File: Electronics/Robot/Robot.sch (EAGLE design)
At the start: 23 parts, among them Q1 2N7000, Q2 2N7000, U1 GY-521MPU6050, U2 SN74LS241N

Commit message: Fixed Gears and made PCB
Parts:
- removed JP1: B3B-PH-K-S, con-JST PH:B3B-PH-K-S
- added X2: JST-XH-03-PIN-ROUND-PAD, JST XH Connectors v1-0:JST-XH-03-PIN-ROUND-PAD
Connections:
- net ENABLE_AX12: now also U$1.20/A6/TX5
- net GND: now also X2-3.S; no longer JP1.3
- net RX_AX12: now also U$1.17/A3/TX4/SDA1
- net SSC-32-RX: now also X2-2.S; no longer JP1.2
- net SSC-32-TX: now also X2-1.S; no longer JP1.1
- net TX_AX12: now also U$1.16/A2/RX4/SCL1
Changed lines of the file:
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@@
 <?xml version="1.0" encoding="utf-8"?>
 <!DOCTYPE eagle SYSTEM "eagle.dtd">
-<eagle version="9.6.1">
+<eagle version="9.6.2">
 <drawing>
 <settings>
@@
 <part name="+3V4" library="supply1" library_urn="urn:adsk.eagle:library:371" deviceset="+3V3" device=""/>
 <part name="P+4" library="supply1" library_urn="urn:adsk.eagle:library:371" deviceset="+5V" device=""/>
-<part name="JP1" library="con-JST PH" deviceset="B3B-PH" device="-K-S"/>
 <part name="GND1" library="supply1" library_urn="urn:adsk.eagle:library:371" deviceset="GND" device=""/>
 <part name="H1" library="holes" library_urn="urn:adsk.eagle:library:237" deviceset="MOUNT-HOLE" device="3.0" package3d_urn="urn:adsk.eagle:package:14277/1"/>
@@
 <part name="GND4" library="supply1" library_urn="urn:adsk.eagle:library:371" deviceset="GND" device=""/>
 <part name="U$1" library="Teensy_3_and_LC_Series_Boards_v1.4" deviceset="TEENSY_4.0" device=""/>
+<part name="X2" library="JST XH Connectors v1-0" deviceset="JST-XH-03-PIN" device="-ROUND-PAD"/>
 </parts>
 <sheets>
@@
 <attribute name="VALUE" x="299.72" y="238.76" size="1.778" layer="96" rot="R90"/>
 </instance>
-<instance part="JP1" gate="G$1" x="358.14" y="149.86" smashed="yes" rot="R180">
-<attribute name="NAME" x="364.49" y="144.145" size="1.778" layer="95" rot="R180"/>
-<attribute name="VALUE" x="364.49" y="157.48" size="1.778" layer="96" rot="R180"/>
-</instance>
 <instance part="GND1" gate="1" x="345.44" y="137.16" smashed="yes" rot="MR0">
 <attribute name="VALUE" x="347.98" y="134.62" size="1.778" layer="96" rot="MR0"/>
@@
 <attribute name="NAME" x="52.832" y="229.87" size="1.27" layer="95" font="vector" ratio="15"/>
 <attribute name="VALUE" x="55.626" y="157.48" size="1.27" layer="96" font="vector" ratio="15"/>
+</instance>
+<instance part="X2" gate="-1" x="353.06" y="152.4" smashed="yes">
+<attribute name="NAME" x="355.6" y="151.638" size="1.524" layer="95"/>
+<attribute name="VALUE" x="352.298" y="153.797" size="1.778" layer="96"/>
+</instance>
+<instance part="X2" gate="-2" x="353.06" y="149.86" smashed="yes">
+<attribute name="NAME" x="355.6" y="149.098" size="1.524" layer="95"/>
+</instance>
+<instance part="X2" gate="-3" x="353.06" y="147.32" smashed="yes">
+<attribute name="NAME" x="355.6" y="146.558" size="1.524" layer="95"/>
 </instance>
 </instances>
@@
 <pinref part="GND1" gate="1" pin="GND"/>
 <wire x1="345.44" y1="139.7" x2="345.44" y2="147.32" width="0.1524" layer="91"/>
-<pinref part="JP1" gate="G$1" pin="3"/>
 <wire x1="345.44" y1="147.32" x2="350.52" y2="147.32" width="0.1524" layer="91"/>
+<pinref part="X2" gate="-3" pin="S"/>
 </segment>
 <segment>
@@
 <net name="SSC-32-RX" class="0">
 <segment>
-<pinref part="JP1" gate="G$1" pin="2"/>
 <wire x1="350.52" y1="149.86" x2="345.44" y2="149.86" width="0.1524" layer="91"/>
 <label x="345.44" y="149.86" size="1.016" layer="95" rot="R180" xref="yes"/>
+<pinref part="X2" gate="-2" pin="S"/>
 </segment>
 <segment>
@@
 <net name="SSC-32-TX" class="0">
 <segment>
-<pinref part="JP1" gate="G$1" pin="1"/>
 <wire x1="350.52" y1="152.4" x2="345.44" y2="152.4" width="0.1524" layer="91"/>
 <label x="345.44" y="152.4" size="1.016" layer="95" rot="R180" xref="yes"/>
+<pinref part="X2" gate="-1" pin="S"/>
 </segment>
 <segment>
@@
 <label x="27.94" y="165.1" size="1.016" layer="95" rot="R180" xref="yes"/>
 <pinref part="U$1" gate="G$1" pin="23/A9/PWM"/>
+</segment>
+</net>
+<net name="TX_AX12" class="0">
+<segment>
+<pinref part="U$1" gate="G$1" pin="16/A2/RX4/SCL1"/>
+<wire x1="35.56" y1="182.88" x2="27.94" y2="182.88" width="0.1524" layer="91"/>
+<label x="27.94" y="182.88" size="1.016" layer="95" rot="R180" xref="yes"/>
+</segment>
+</net>
+<net name="RX_AX12" class="0">
+<segment>
+<pinref part="U$1" gate="G$1" pin="17/A3/TX4/SDA1"/>
+<wire x1="35.56" y1="180.34" x2="27.94" y2="180.34" width="0.1524" layer="91"/>
+<label x="27.94" y="180.34" size="1.016" layer="95" rot="R180" xref="yes"/>
+</segment>
+</net>
+<net name="ENABLE_AX12" class="0">
+<segment>
+<pinref part="U$1" gate="G$1" pin="20/A6/TX5"/>
+<wire x1="35.56" y1="172.72" x2="27.94" y2="172.72" width="0.1524" layer="91"/>
+<label x="27.94" y="172.72" size="1.016" layer="95" rot="R180" xref="yes"/>
 </segment>
 </net>
@@
 <wire x1="127" y1="175.26" x2="127" y2="132.08" width="0.1524" layer="91"/>
 <wire x1="127" y1="132.08" x2="165.1" y2="132.08" width="0.1524" layer="91"/>
-<label x="101.6" y="175.26" size="1.778" layer="95"/>
+<label x="96.52" y="175.26" size="1.778" layer="95" rot="R180" xref="yes"/>
 </segment>
 </net>
@@
 <wire x1="121.92" y1="170.18" x2="121.92" y2="114.3" width="0.1524" layer="91"/>
 <wire x1="96.52" y1="170.18" x2="121.92" y2="170.18" width="0.1524" layer="91"/>
-<label x="101.6" y="170.18" size="1.778" layer="95"/>
 <wire x1="203.2" y1="114.3" x2="203.2" y2="165.1" width="0.1524" layer="91"/>
 <pinref part="U2" gate="A" pin="1Y1"/>
 <wire x1="203.2" y1="165.1" x2="200.66" y2="165.1" width="0.1524" layer="91"/>
 <wire x1="121.92" y1="114.3" x2="203.2" y2="114.3" width="0.1524" layer="91"/>
+<label x="96.52" y="170.18" size="1.778" layer="95" rot="R180" xref="yes"/>
 </segment>
 </net>
@@
 <wire x1="162.56" y1="157.48" x2="165.1" y2="157.48" width="0.1524" layer="91"/>
 <junction x="162.56" y="160.02"/>
-<label x="101.6" y="165.1" size="1.778" layer="95"/>
-</segment>
-</net>
+<label x="96.52" y="165.1" size="1.778" layer="95" rot="R180" xref="yes"/>
+</segment>
+</net>

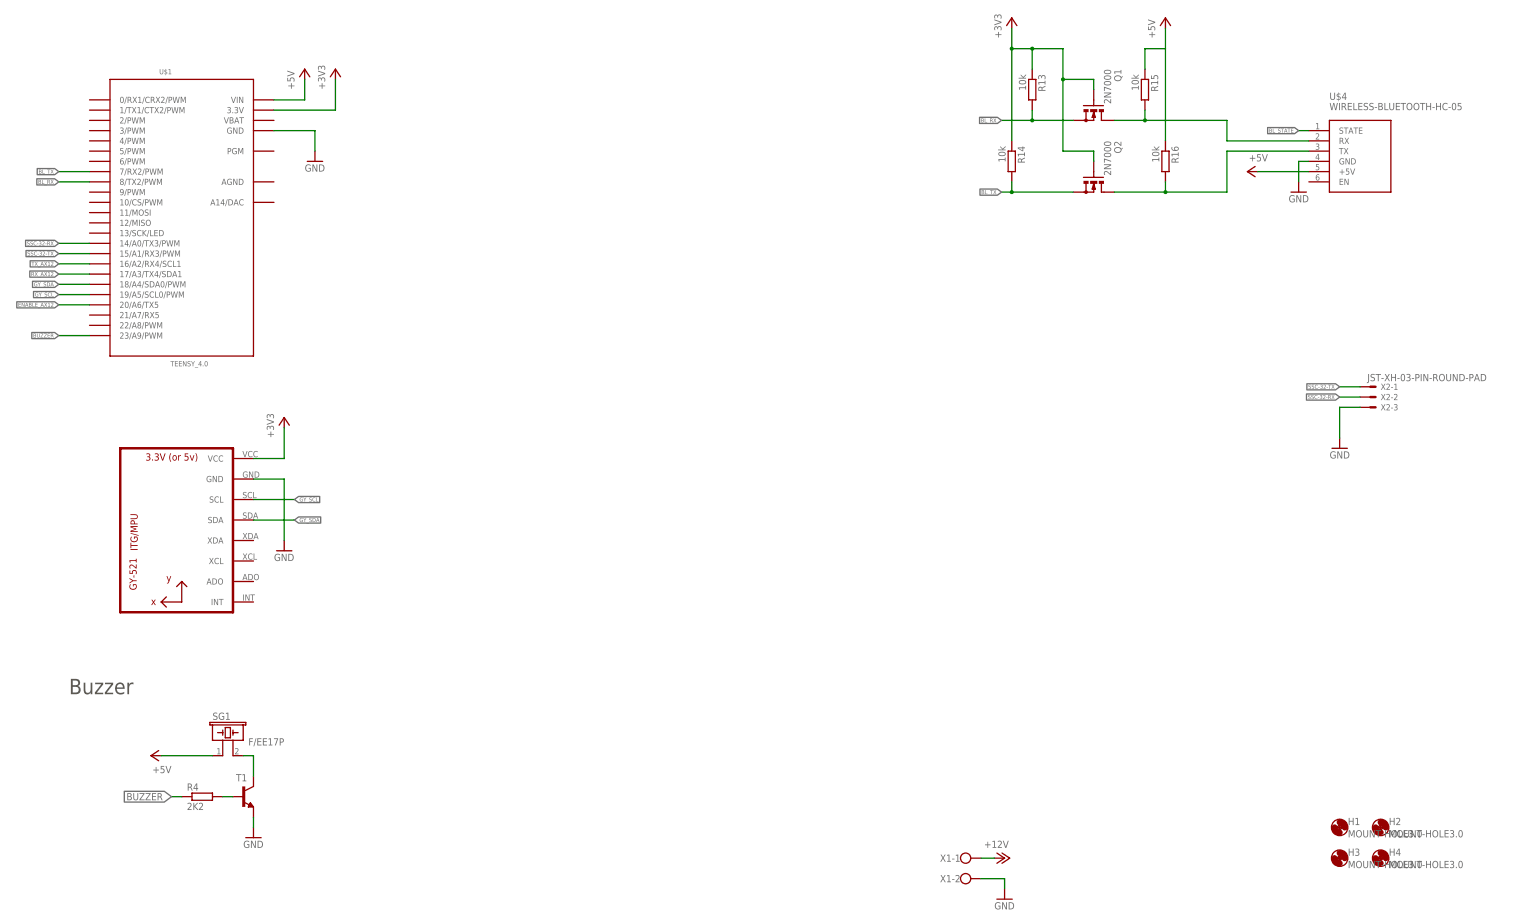
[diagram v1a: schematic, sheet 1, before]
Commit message: 5V added & better layout
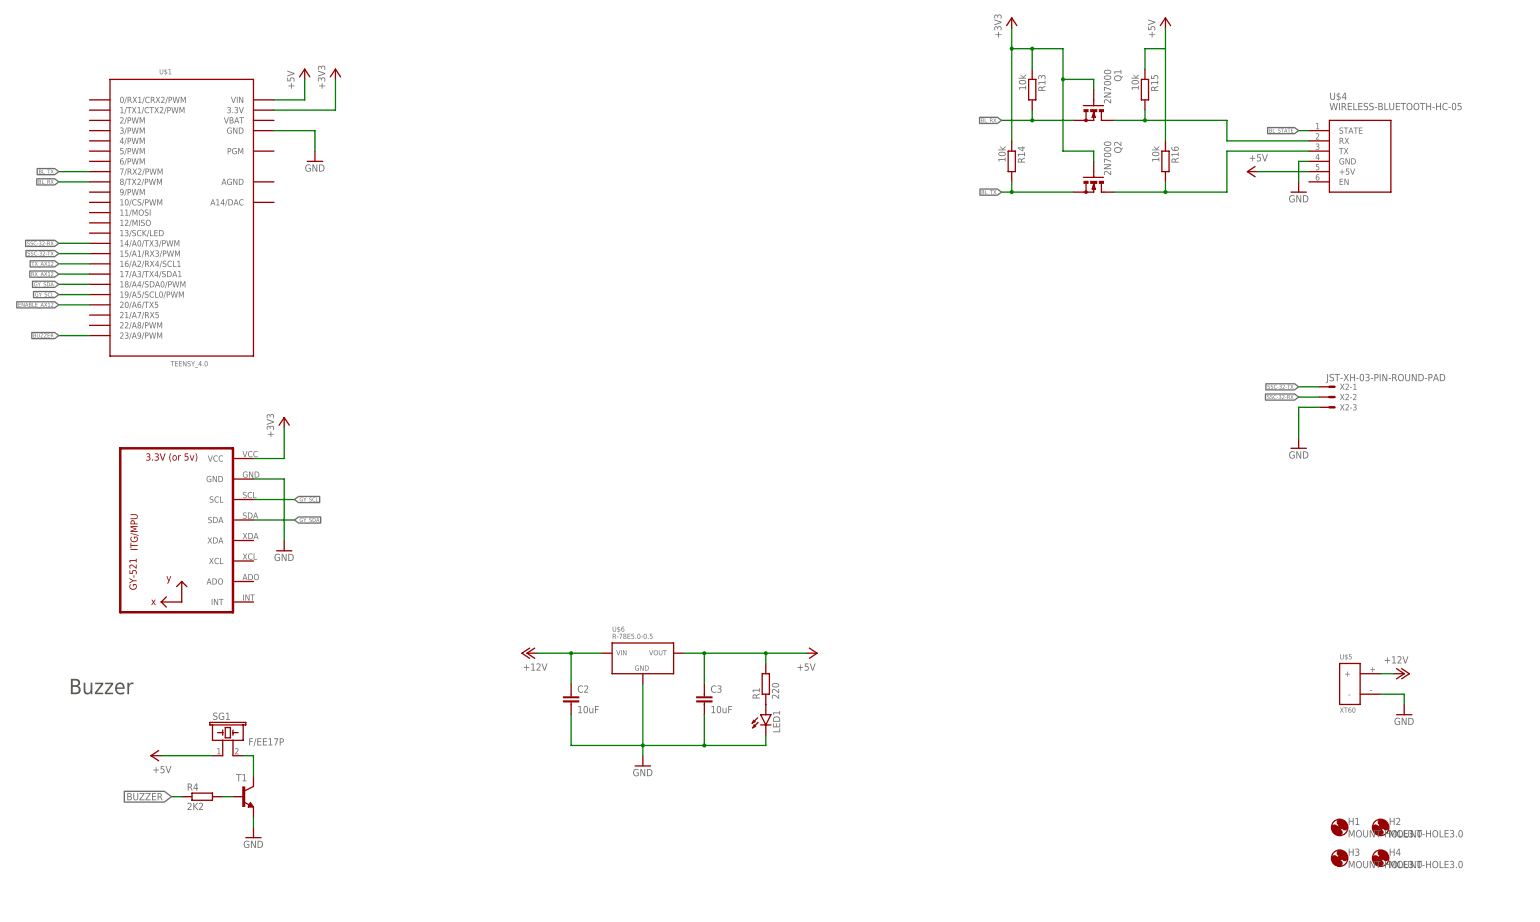
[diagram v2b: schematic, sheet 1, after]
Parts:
- removed X1: (no value), con-wago-500:W237-102
- added C2, C3: 10uF, rcl:C-EU050-024X044
- added LED1: (no value), led:LED5MM
- added R1: 220, rcl:R-EU_0207/10
- added U$5: XT60, XT60:XT60
- added U$6: R-78E5.0-0.5, Power:R-78E5.0-0.5
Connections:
- new net N$5: LED1.A, R1.1
- net +12V: now also C2.1, U$5.+, U$6.VIN; no longer X1-1.KL
- net +5V: now also C3.1, R1.2, U$6.VOUT
- net GND: now also C2.2, C3.2, LED1.C, U$5.-, U$6.GND; no longer X1-2.KL
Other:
- moved on the sheet: X2-1, X2-2, X2-3
